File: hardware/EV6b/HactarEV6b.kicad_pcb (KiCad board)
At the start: 4 copper layers, 72.7 x 89.4 mm, 116 parts, among them J1 Conn_01x02_Female, J10 Conn_01x08_Female, J11 Conn_01x06_Female, J12 Conn_01x04_Female, J13 Conn_01x04_Female, J14 Conn_01x04_Female, J15 Conn_01x02_Female, J2 Conn_01x02_Female, J3 Conn_01x04_Female, J4 Conn_01x08_Male, J5 Conn_01x04_Female, J6 Conn_01x04_Female, J7 Conn_01x04_Female, J8 Conn_01x06_Female, J9 USB_C_Receptacle, SW1 SW_Push, SW2 SW_Push, SW3 SW_Push, U1 STM32F446RET6, U11 ESP32-S3-WROOM-1-N8R2, U12 MCP73832-2-OT, U13 BM14B(0.8)-24DS-0.4V(53), U2 AMS1117-3.3, U3 CH340C, U4 USBLC6-2P6, U5 STM32F091CCT6, U6 WM8960CGEFL/RV, Y1 Crystal_GND24

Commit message: move to new name and add LCSC part numbers
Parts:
- C23, C4: value 33P -> 33p
- C28, C3, C31, C6: value 4.7u -> 4u7
- C29, C30: value 100U -> 100u
- R11, R12, R14, R15, R17, R18, R24, R25, R34, R35: value 150 -> 150r
- R13, R16, R23, R33, R6: value 180 -> 180r
- R22, R26, R27, R28, R29, R30, R31: value 330 -> 330r
- R40, R41: value 1R0 -> 1r0

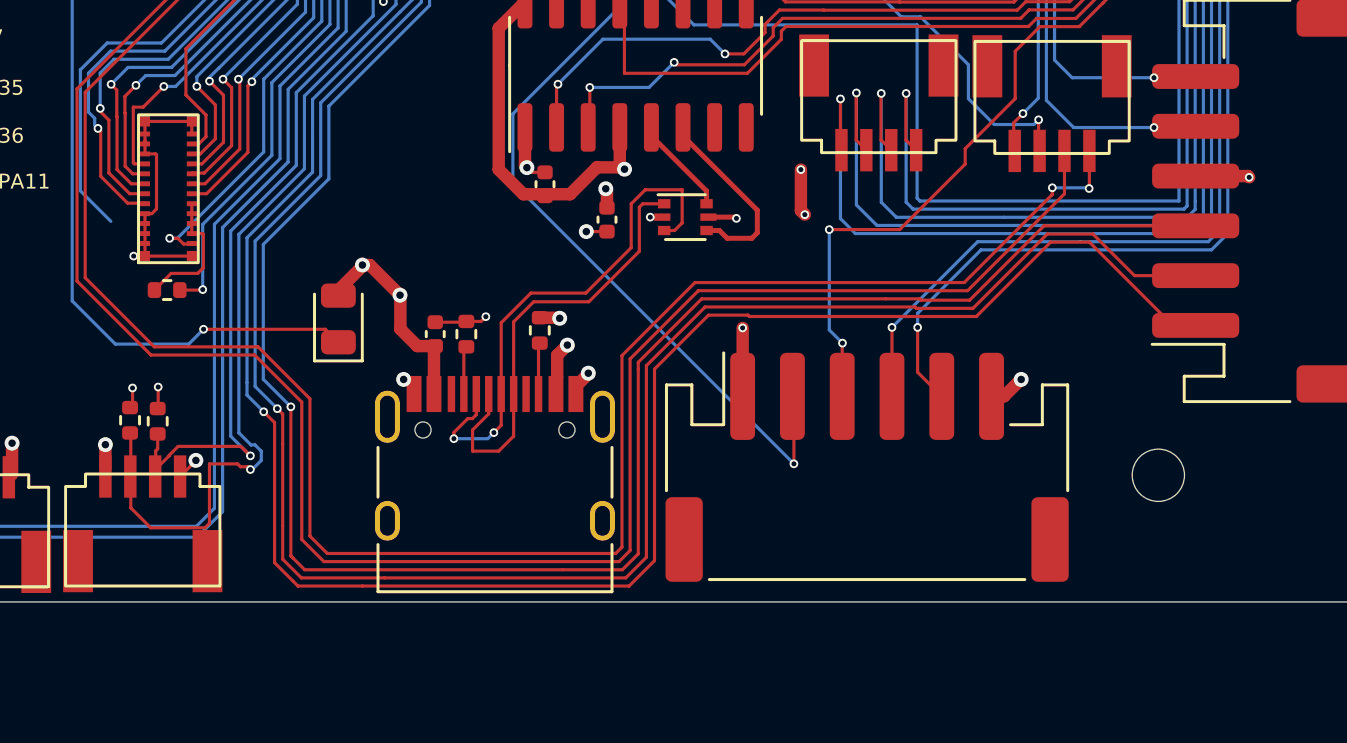
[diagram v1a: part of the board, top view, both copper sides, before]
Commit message: move to new USB connector
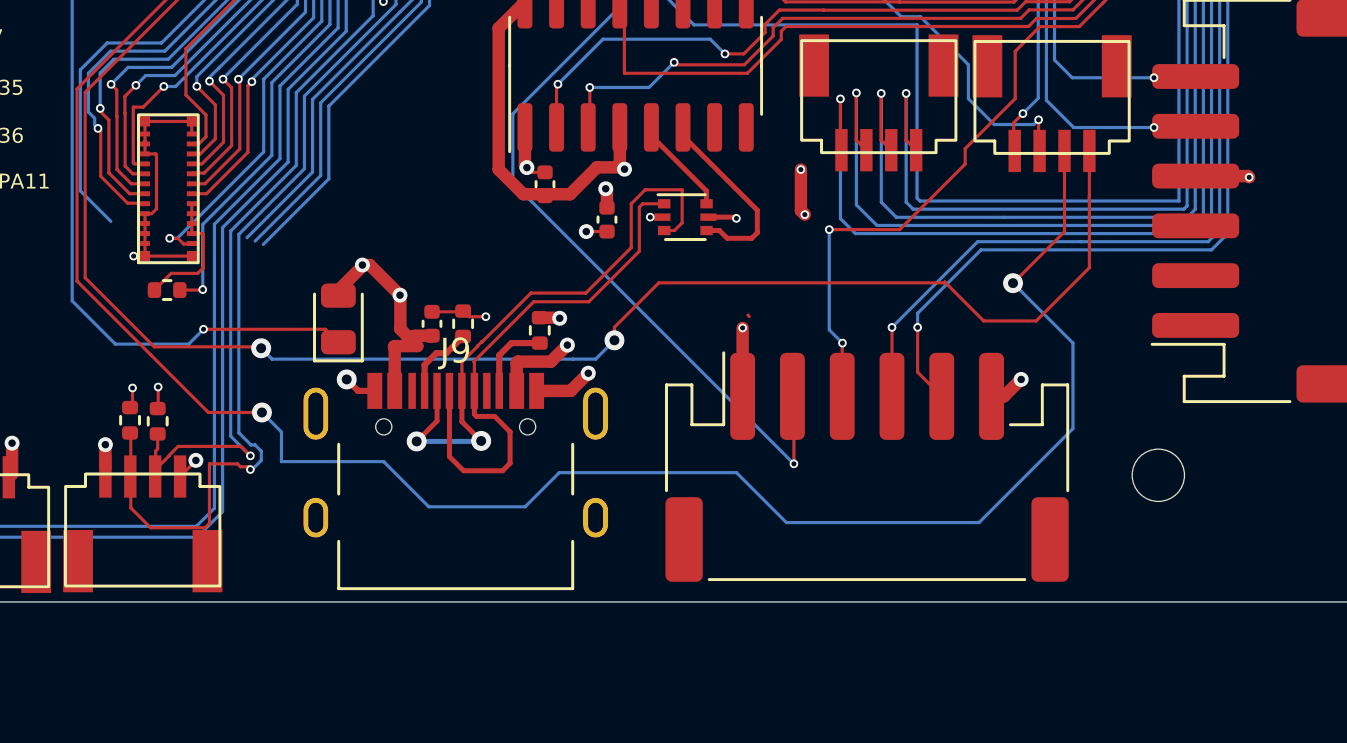
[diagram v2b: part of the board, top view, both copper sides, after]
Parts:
- J9: footprint Connector_USB:USB_C_Receptacle_HRO_TYPE-C-31-M-12 -> PartLibrary:USB_C_Receptacle_HRO_TYPE-C-31-M-13
- moved J9 1.58 mm to (148.7, 141.0)
- moved C1 0.44 mm to (147.8, 134.3)
- moved R3 0.44 mm to (149.0, 134.3)
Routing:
- net /MIC_P: track 98.3 -> 36.7 mm, vias 2 -> 1
- net /MIC_N: track 92.6 -> 31.4 mm, vias 2 -> 1
- net /IN_3: track 91.9 -> 32.0 mm, vias 4 -> 3
- net /UI_SWDIO: track 93.3 -> 82.6 mm
- net /USB_D+: track 18.1 -> 21.9 mm
- net VBUS: track 77.5 -> 80.4 mm
- net /USB_D-: track 21.2 -> 23.4 mm
- net GND: track 692.6 -> 694.7 mm
- net Net-(J9-CC1): track 1.94 -> 3.21 mm
- net Net-(J9-CC2): track 2.07 -> 3.33 mm
- net /UI_SWDCLK: track 88.8 -> 89.3 mm, vias 0 -> 2
